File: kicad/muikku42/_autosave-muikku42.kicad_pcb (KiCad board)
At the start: 2 copper layers, 152.4 x 96.4 mm, 31 parts, among them U1 Raspberry_Pi_Pico, U2 TRRS, U3 TRRS

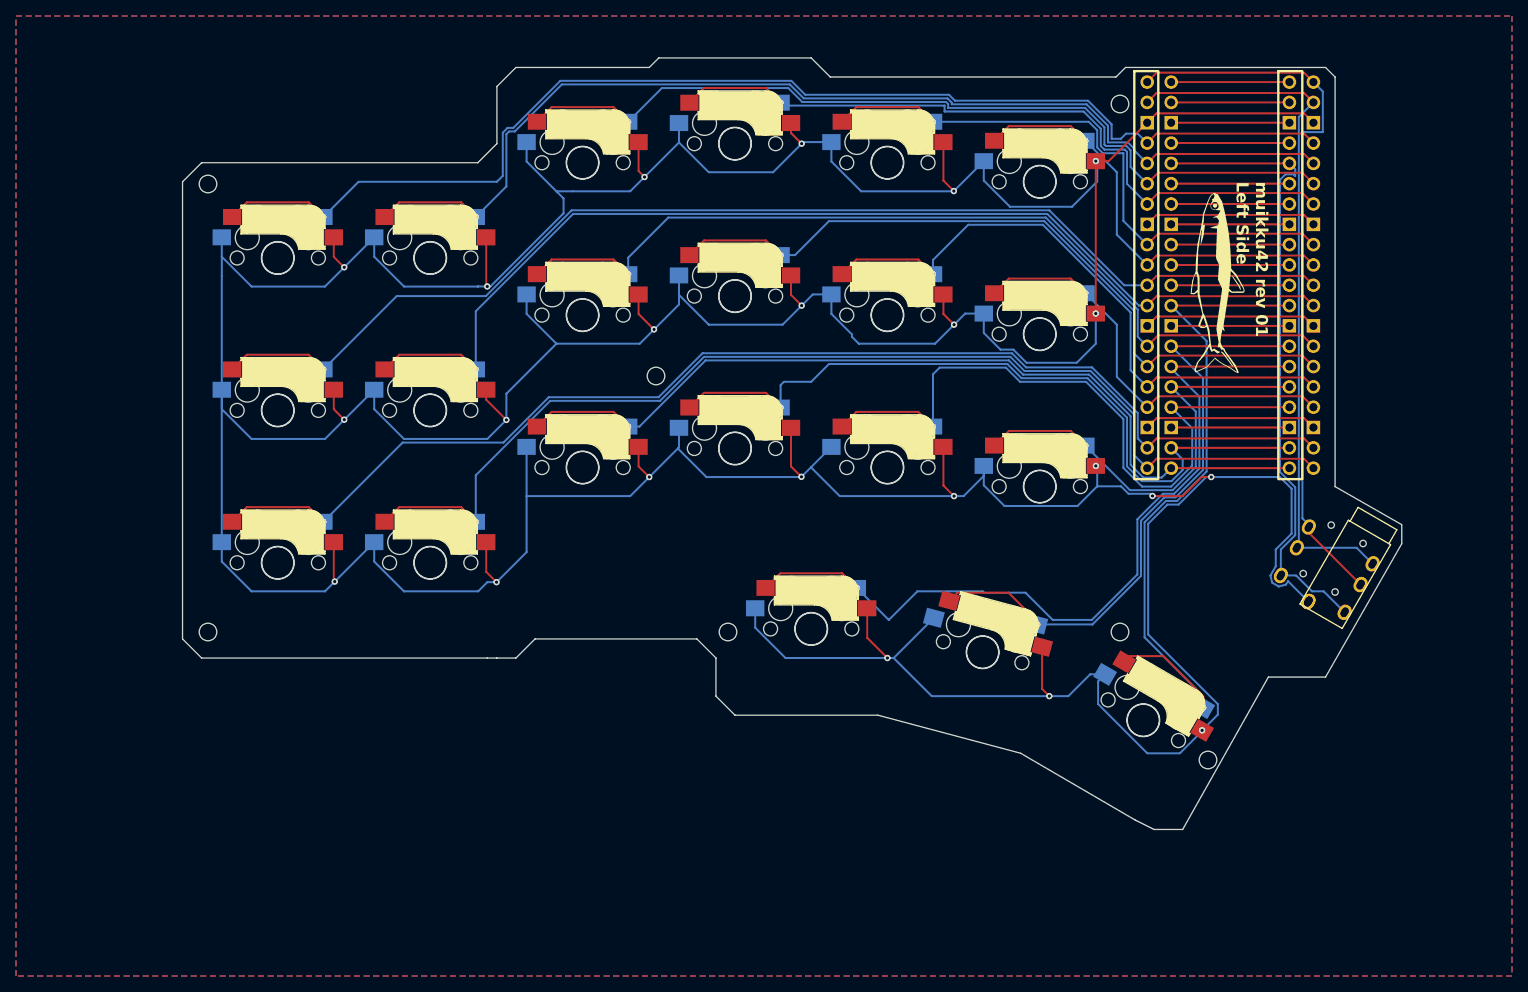
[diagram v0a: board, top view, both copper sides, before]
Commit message: New PCB design and new info
Everything has been updated, much simpler and cheaper design
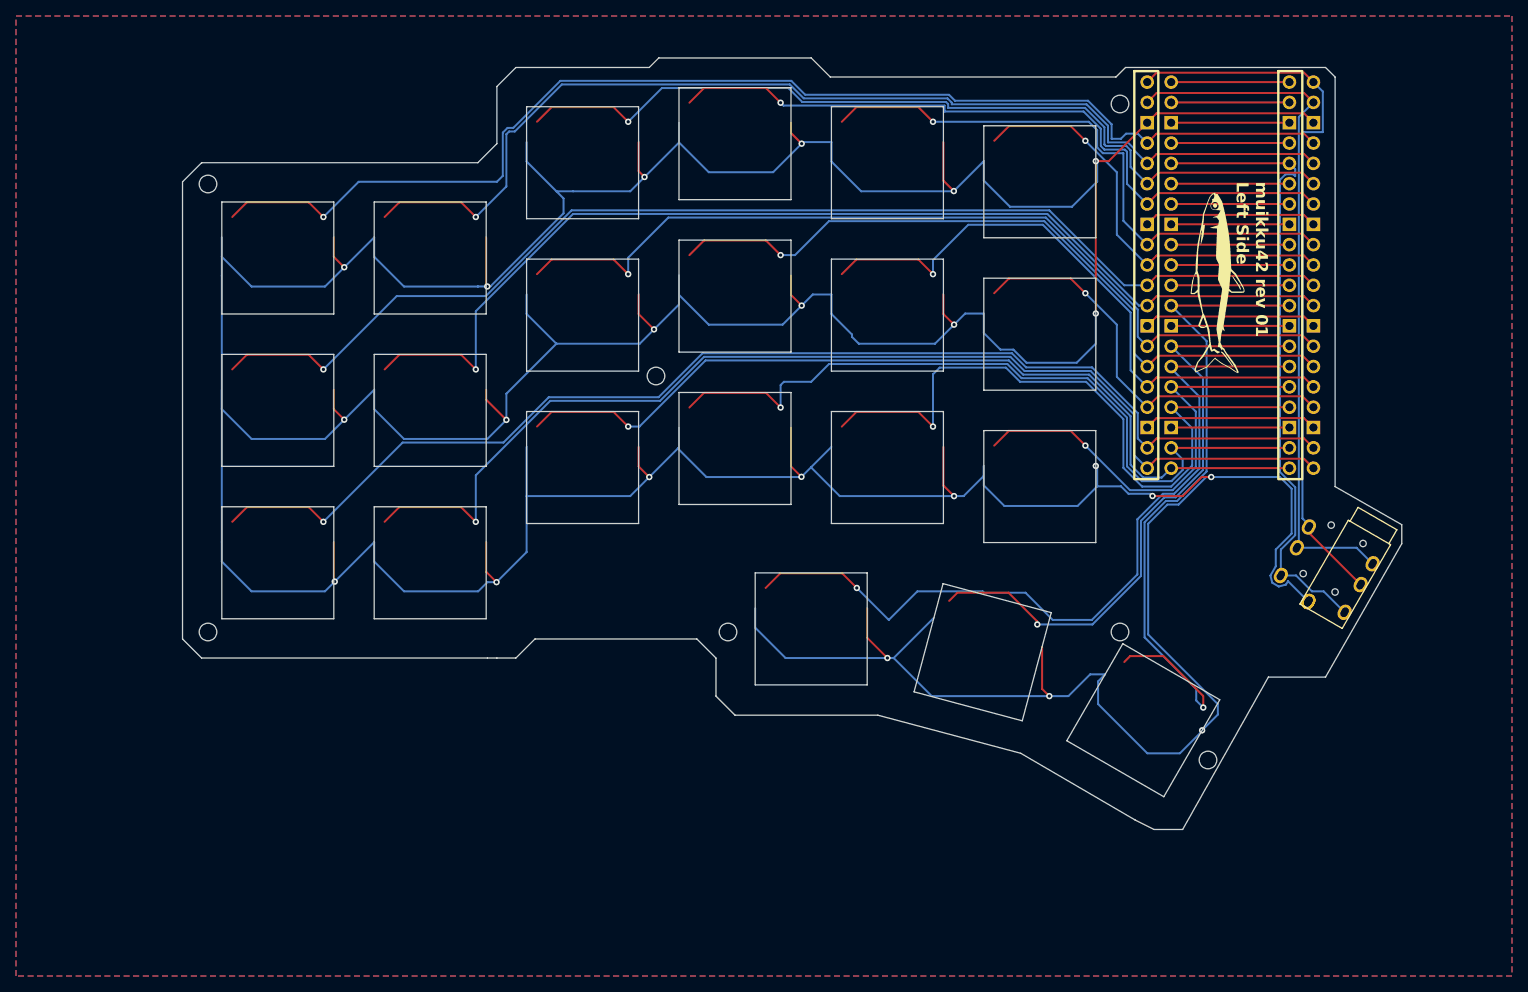
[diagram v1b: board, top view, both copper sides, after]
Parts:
- S1, S10, S11, S12, S13, S14, S15, S16, S17, S18, S19, S2, S20, S21, S3, S4, S5, S6, S7, S8, S9: footprint kbd:CherryMX_MidHeight_Hotswap -> ScottoKeebs_Cutout:Cutout_MX_1.00u
